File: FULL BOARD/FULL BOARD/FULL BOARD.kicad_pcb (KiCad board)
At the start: 2 copper layers, 200 x 200 mm, 100 parts, among them IC1 TAS5760LDAP, J1 PJ-036AH-SMT-TR, J2 Micro_SD_Card, J3 B2B-PH-K-S, J4 5019514000, J5 61201021621, J6 B2B-PH-K-S, SW1 SW_Push, U1 LD1117S33TR_SOT223, U2 STM32H743VITx, Y1 ABLS7M2-16.000MHZ-D-2Y-T

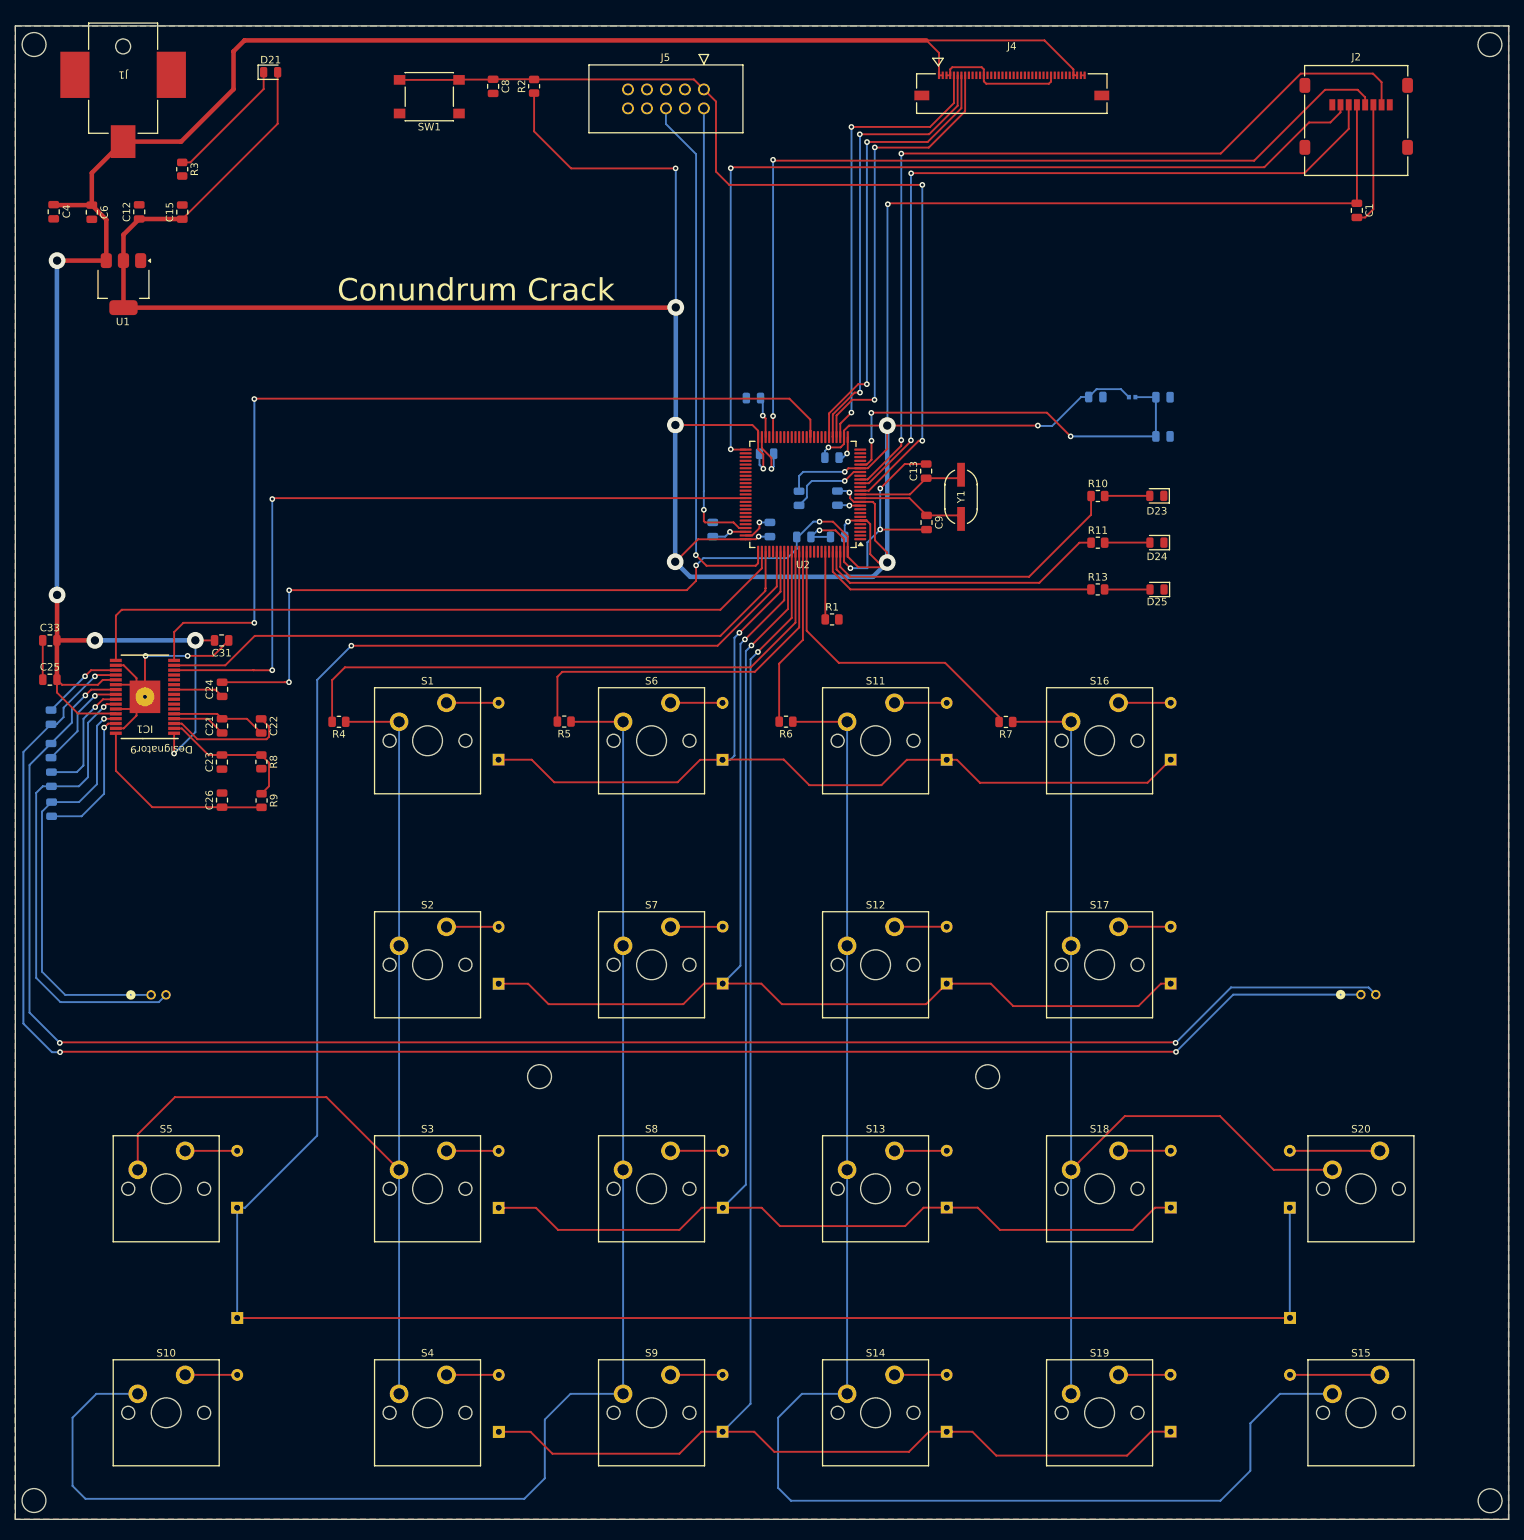
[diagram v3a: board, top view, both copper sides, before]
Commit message: updated footprints
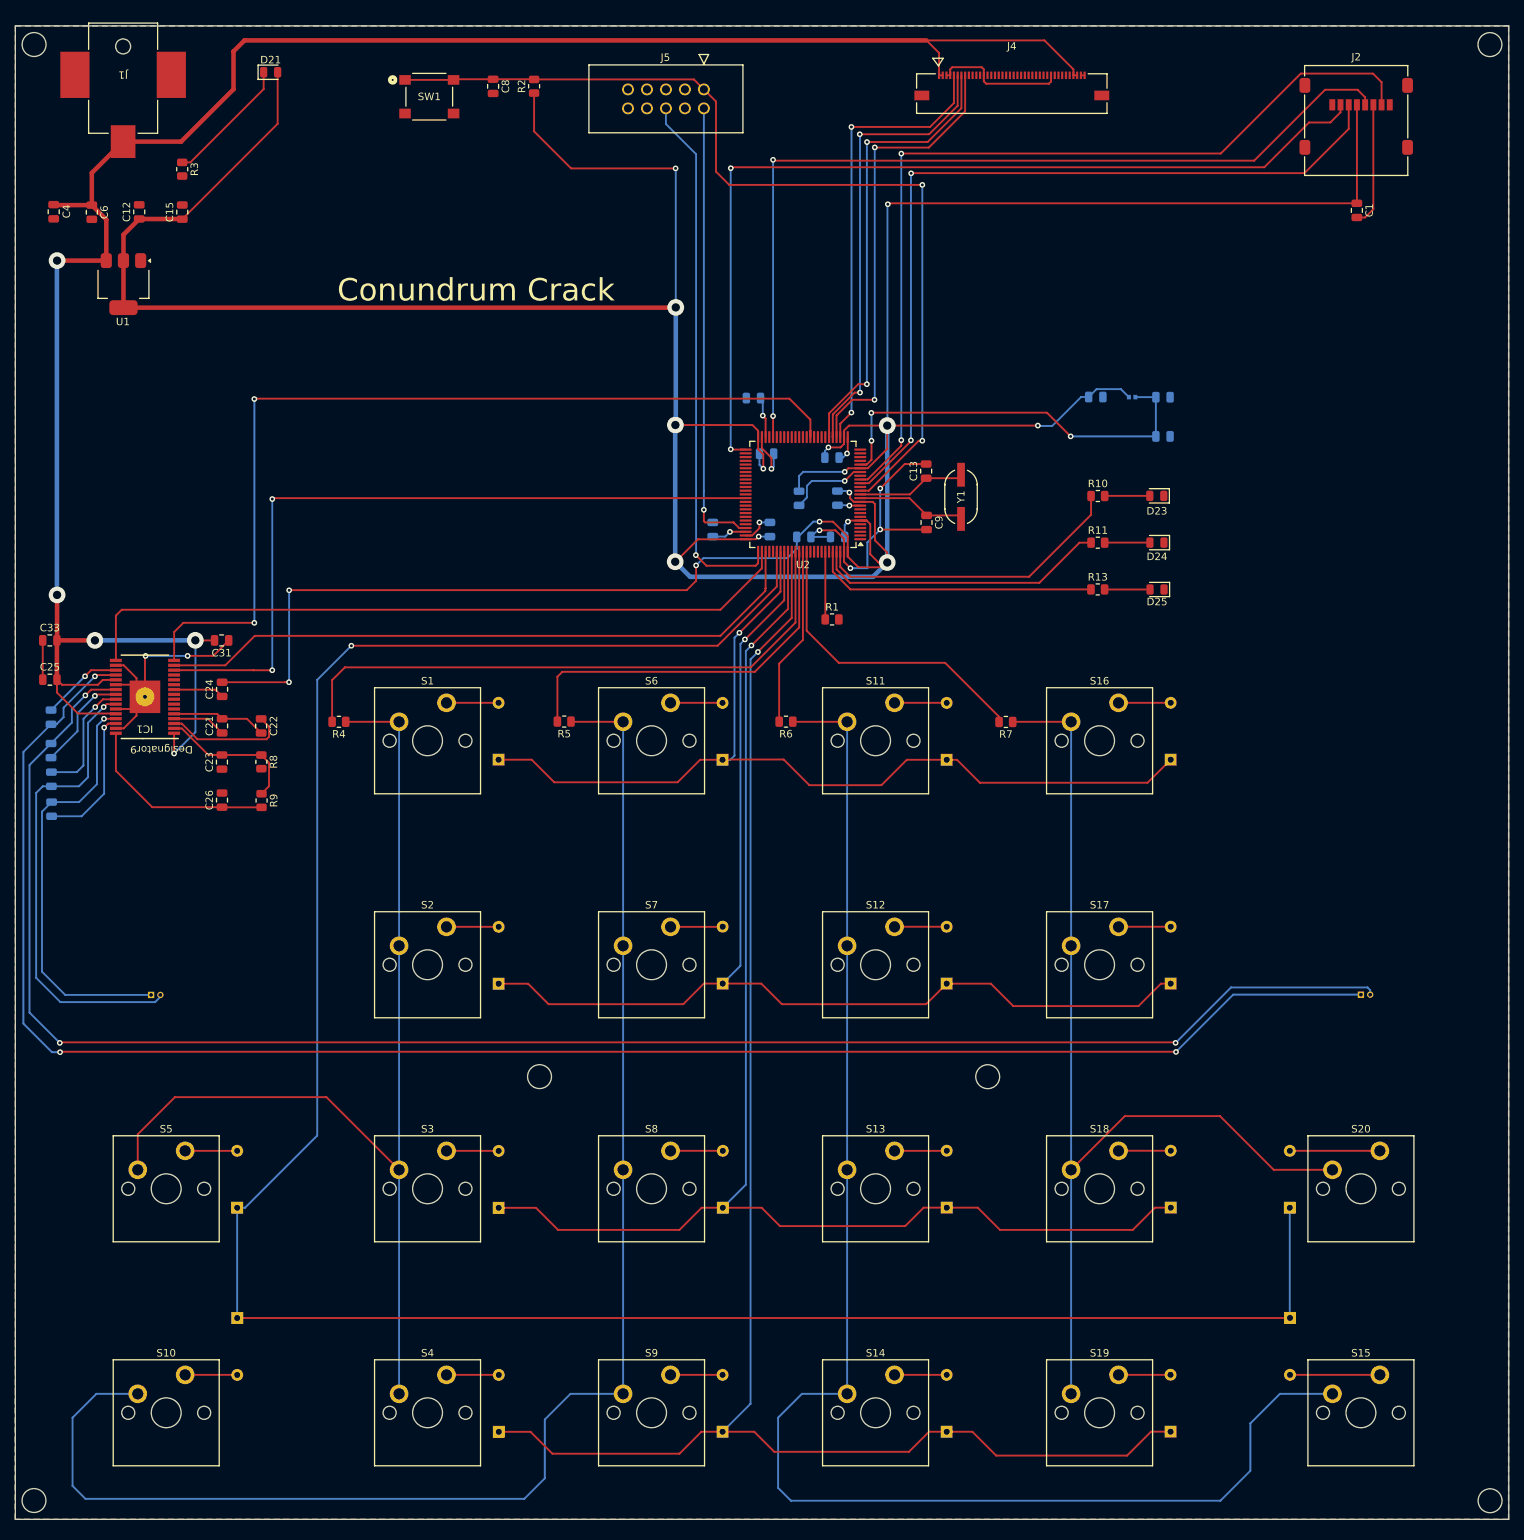
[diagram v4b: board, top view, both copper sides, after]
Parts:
- J3, J6: footprint Audio Jack:CONN2_B2B-PH-K-S_JST -> Audio Connector 2:CON_530470210_MOL
- SW1: value SW_Push -> PTS645SK50SMTR92LFS; footprint Button_Switch_SMD:SW_SPST_PTS645 -> push button custom:SW4_PTS645SK50SMTR92LFS_CNK
- turned SW1 to 0 degrees
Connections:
- SW1 pad 1: GND -> /NRST
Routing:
- net Net-(IC1-SPK_OUTA-): track 63.8 -> 63.2 mm

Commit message: changed LCD footprint, GNDA
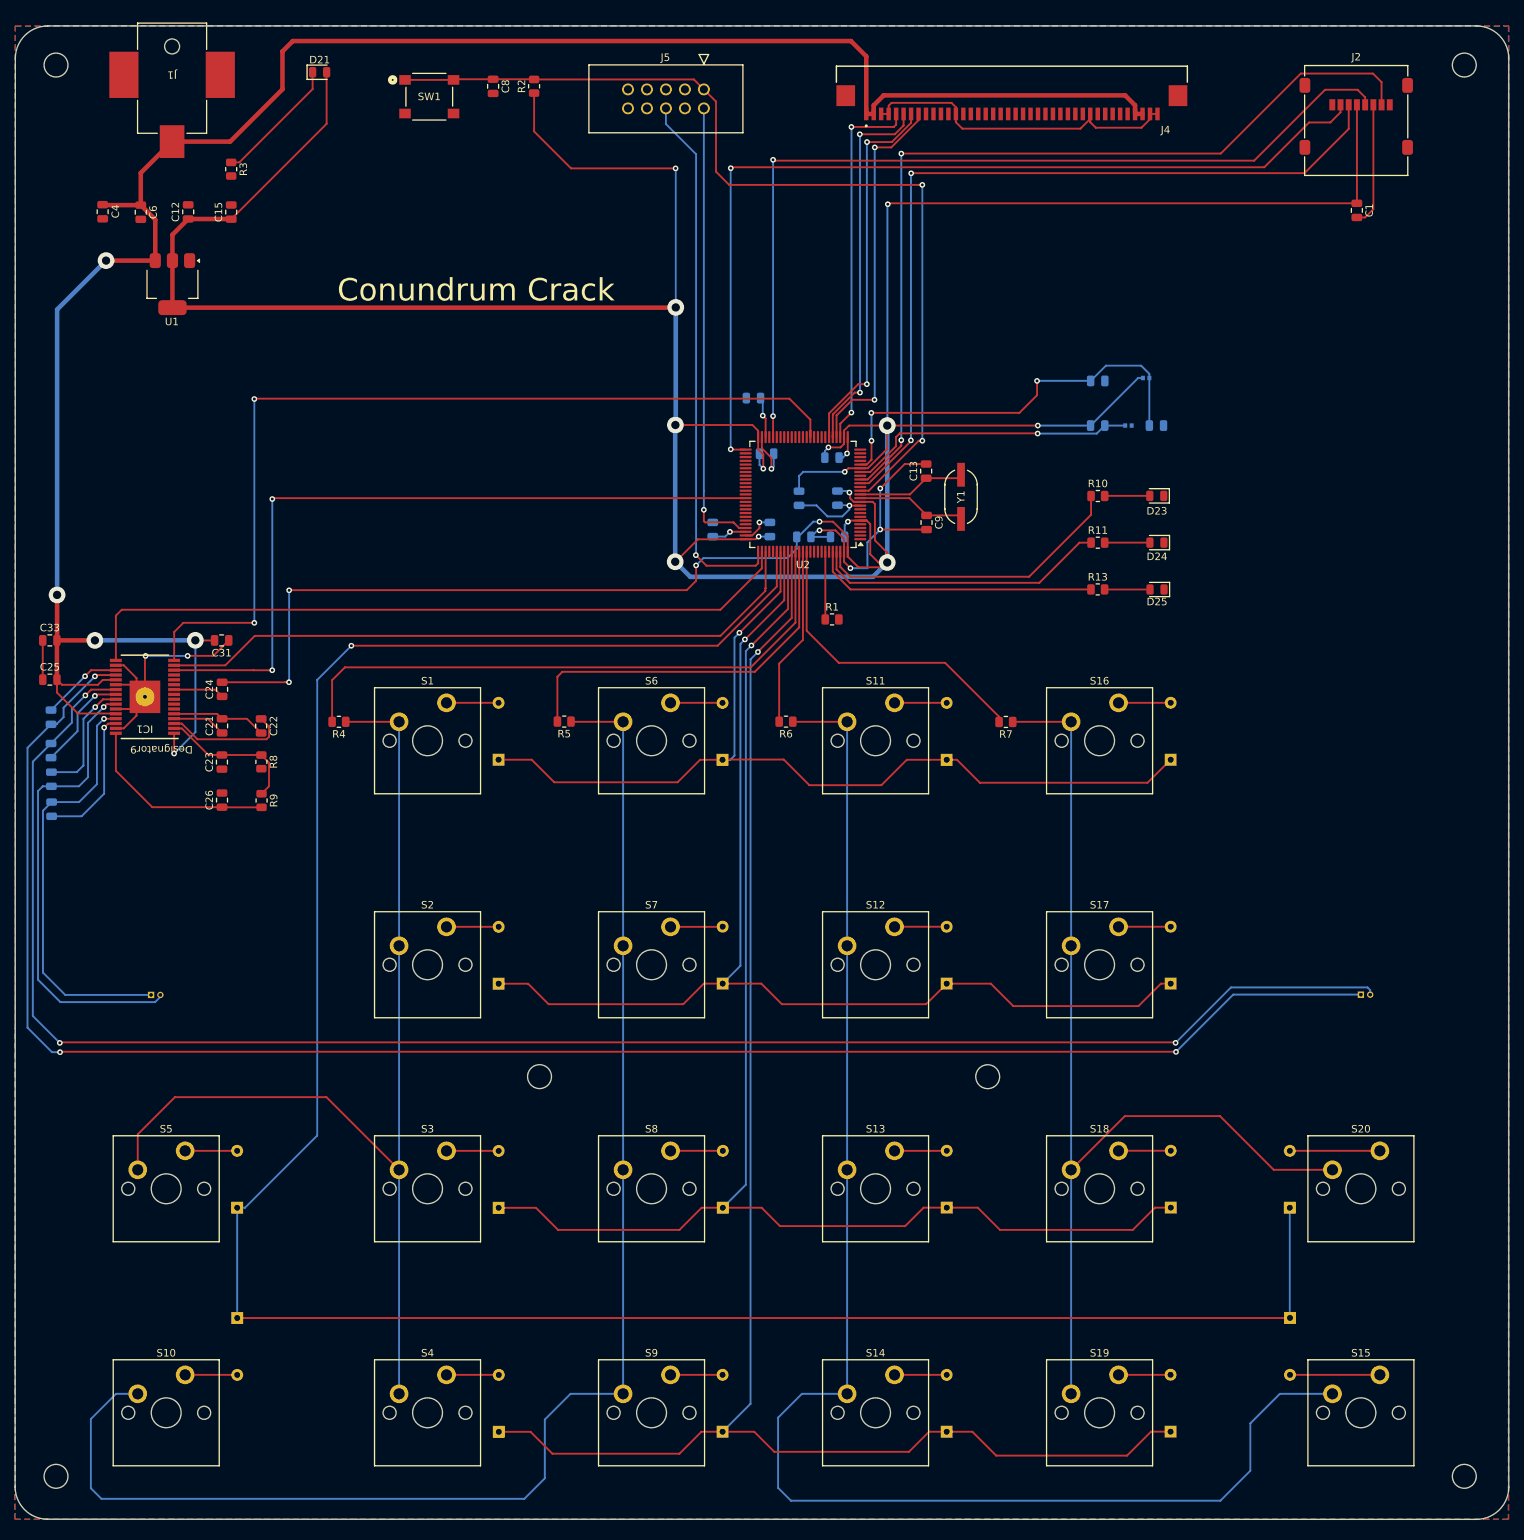
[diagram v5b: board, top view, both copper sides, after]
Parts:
- added FL2: BLM15GA750SZ1D, Ferrite Bead:BEADC1005X55N, B.Cu at (217.6, 97.3)
- J4: footprint real ribbon:CON_5051104091_MOL -> Final Ribbon Connector:GCT_FFC3B07-40-T
- moved C19 9.00 mm to (213.5, 91.3)
- moved C12 6.56 mm to (91.7, 68.7)
- moved C15 6.56 mm to (97.5, 68.7)
- moved D21 6.56 mm to (109.3, 50.0)
- moved J1 6.56 mm to (89.5, 50.8)
- moved R3 6.56 mm to (97.5, 62.9)
- moved C4 6.56 mm to (80.2, 68.6)
- moved C6 6.56 mm to (85.3, 68.7)
- moved U1 6.56 mm to (89.6, 78.3)
- moved C20 3.83 mm to (213.5, 97.3)
- moved FL1 3.18 mm to (220.0, 90.9)
- moved C18 1.69 mm to (221.4, 97.3)
- moved J4 0.27 mm to (202.0, 53.1), turned to 180 degrees
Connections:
- C20 pad 2: GND -> GNDA
- U2 pad 19: GND -> GNDA
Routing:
- net GNDA: track 0.00 -> 38.8 mm, vias 0 -> 1
- net GND: track 141.8 -> 165.5 mm, vias 11 -> 10
- net /LCD_CS: track 60.9 -> 49.7 mm
- net /LCD_MISO: track 61.4 -> 50.5 mm
- net /LCD_MOSI: track 61.2 -> 50.5 mm
- net /LCD_SCK: track 61.6 -> 50.9 mm
- net +5V: track 292.3 -> 300.9 mm
- net Net-(R5-Pad1): track 201.1 -> 196.3 mm
- net +3.3V: track 588.0 -> 583.7 mm
- net +3.3VA: track 55.5 -> 56.4 mm
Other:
- outline, holes or cut-outs redrawn
